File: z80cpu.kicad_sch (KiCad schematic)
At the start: 11 parts

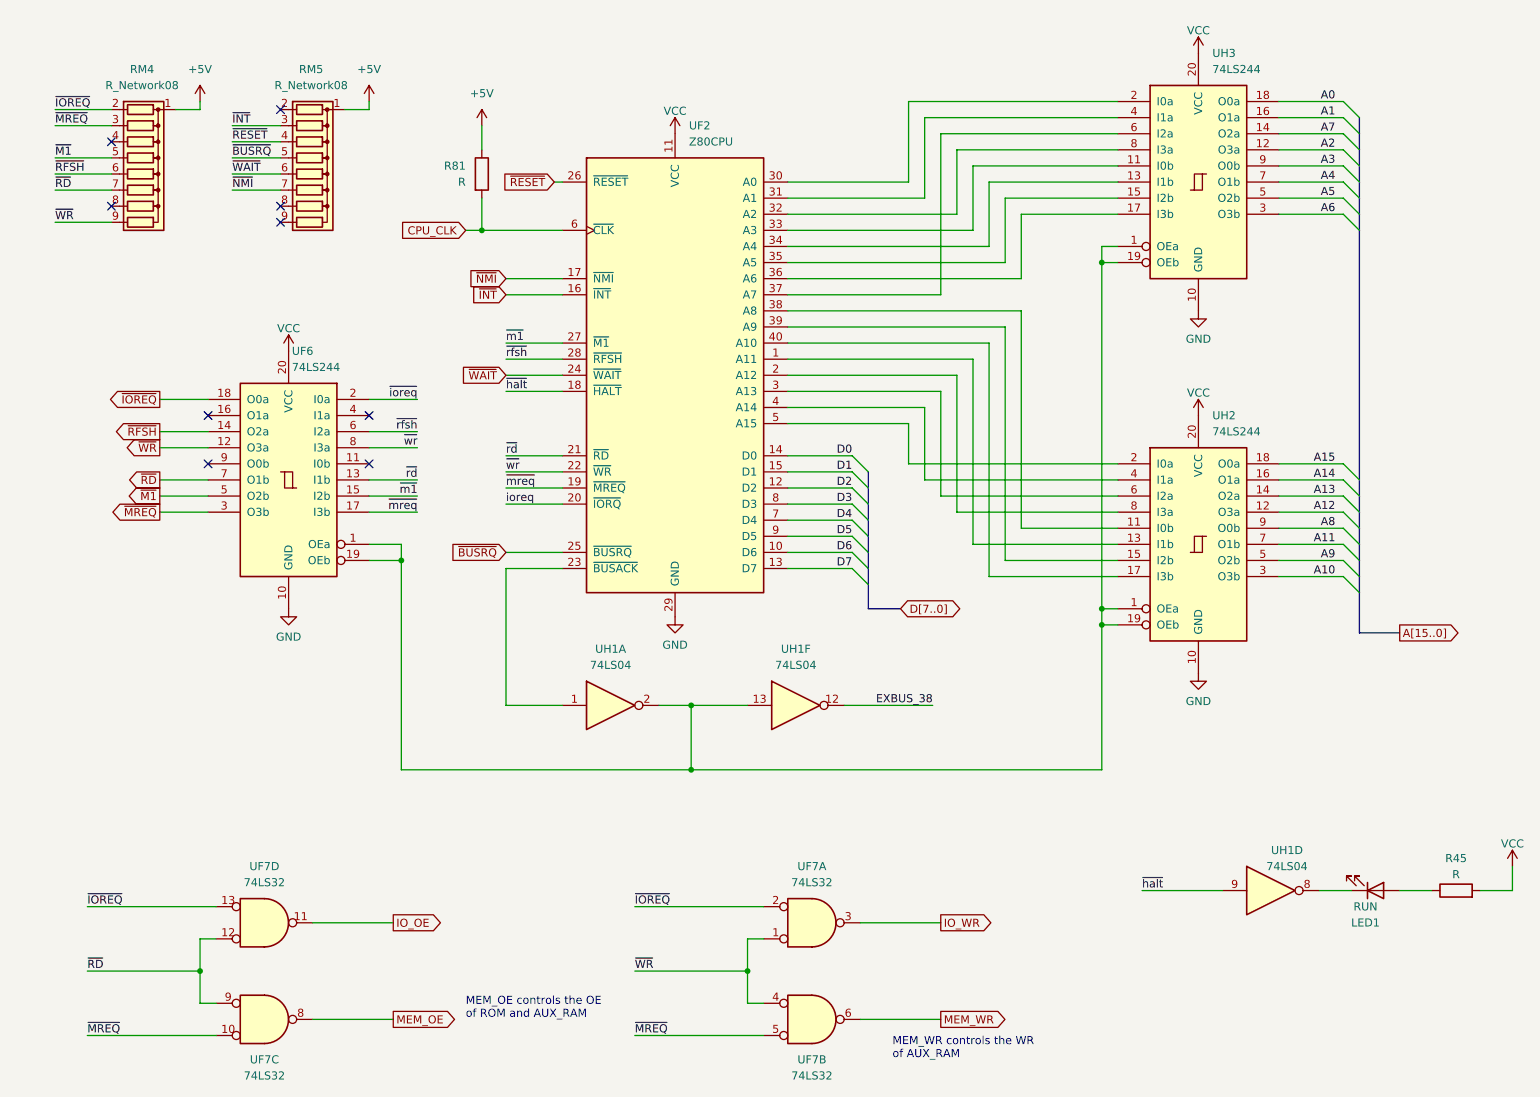
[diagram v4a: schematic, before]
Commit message: VCC -> +5V
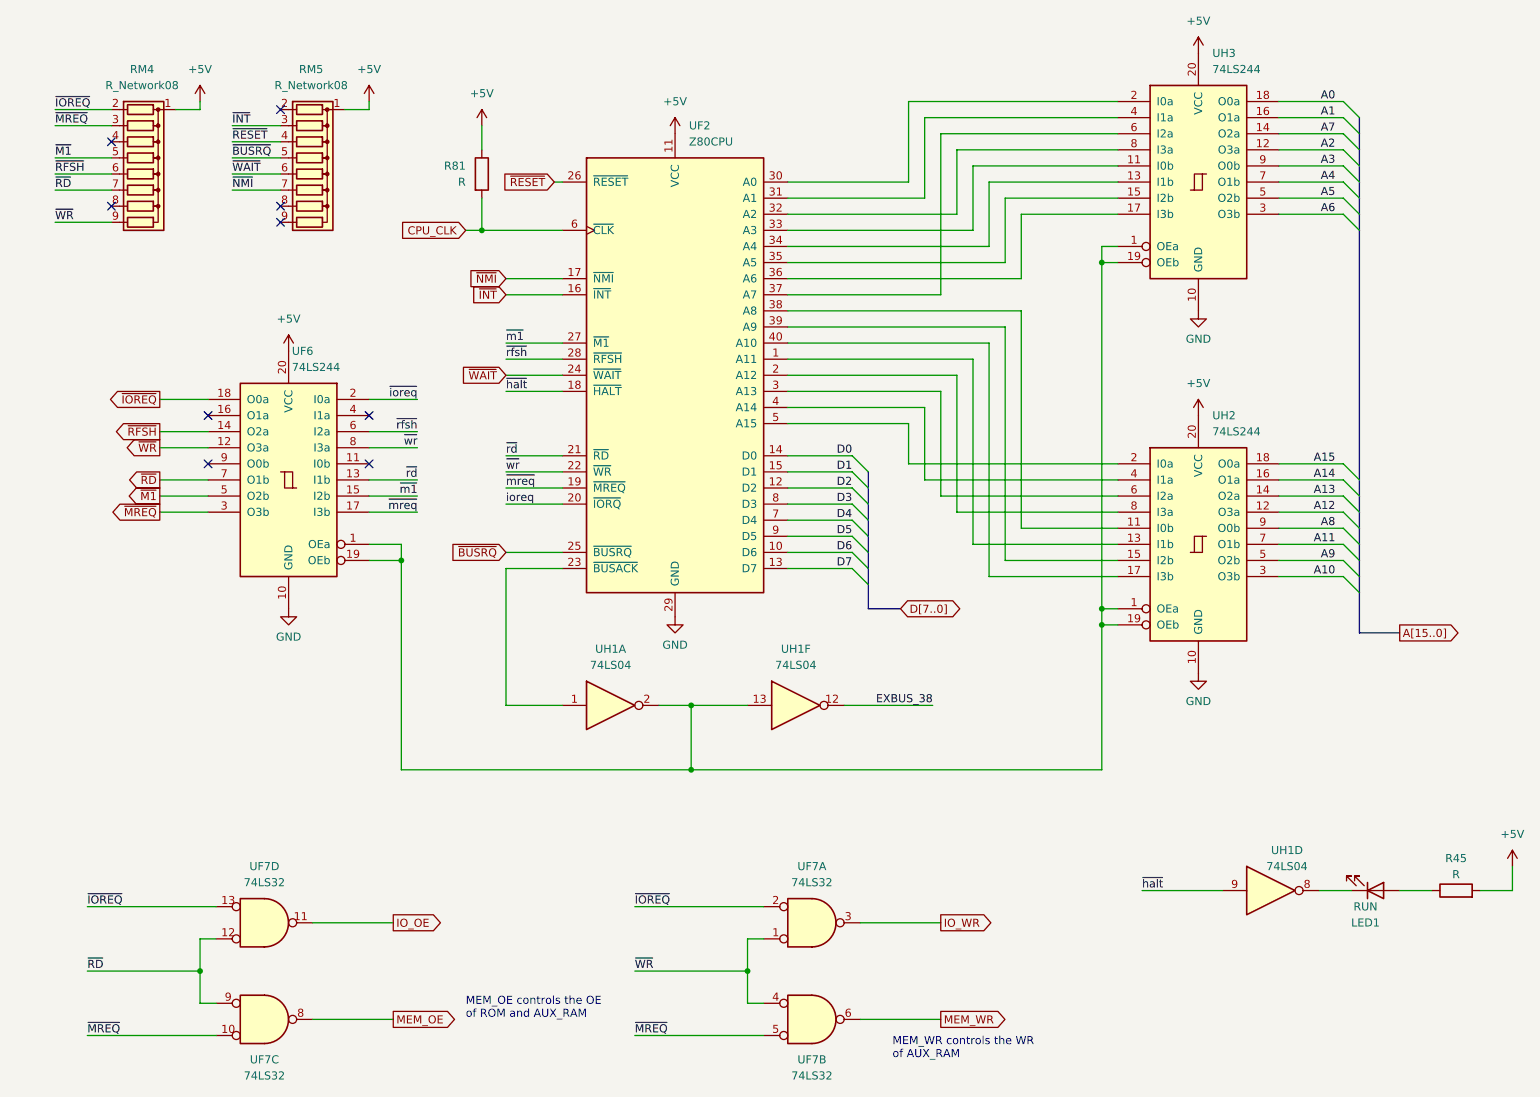
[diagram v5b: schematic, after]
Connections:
- net VCC is gone; now on net +5V: R45.2, UF2.11 (VCC), UF6.20 (VCC), UH2.20 (VCC), UH3.20 (VCC)
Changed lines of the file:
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@@
     )
   )
-  (symbol (lib_id "power:VCC") (at 54.61 68.58 0) (unit 1)
-    (in_bom yes) (on_board yes) (dnp no) (fields_autoplaced)
-    (property "Reference" "#PWR0167" (at 54.61 72.39 0)
-      (effects (font (size 1.27 1.27)) hide)
-    )
-    (property "Value" "VCC" (at 54.61 65.0042 0)
+  (symbol (lib_id "power:+5V") (at 54.61 68.58 0) (unit 1)
+    (in_bom yes) (on_board yes) (dnp no) (fields_autoplaced)
+    (property "Reference" "#PWR?" (at 54.61 72.39 0)
+      (effects (font (size 1.27 1.27)) hide)
+    )
+    (property "Value" "+5V" (at 54.61 63.5 0)
       (effects (font (size 1.27 1.27)))
     )
@@
       (project "ceda"
         (path "/12a6dbe3-008d-4c5b-88f6-9f1c816060be/1847fdc4-53d8-4940-8c5f-7a326599bae2"
-          (reference "#PWR0167") (unit 1)
+          (reference "#PWR?") (unit 1)
         )
       )
@@
     )
   )
-  (symbol (lib_id "power:VCC") (at 115.57 34.29 0) (unit 1)
-    (in_bom yes) (on_board yes) (dnp no) (fields_autoplaced)
-    (property "Reference" "#PWR0163" (at 115.57 38.1 0)
-      (effects (font (size 1.27 1.27)) hide)
-    )
-    (property "Value" "VCC" (at 115.57 30.7142 0)
+  (symbol (lib_id "power:+5V") (at 115.57 34.29 0) (unit 1)
+    (in_bom yes) (on_board yes) (dnp no) (fields_autoplaced)
+    (property "Reference" "#PWR?" (at 115.57 38.1 0)
+      (effects (font (size 1.27 1.27)) hide)
+    )
+    (property "Value" "+5V" (at 115.57 29.21 0)
       (effects (font (size 1.27 1.27)))
     )
@@
       (project "ceda"
         (path "/12a6dbe3-008d-4c5b-88f6-9f1c816060be/1847fdc4-53d8-4940-8c5f-7a326599bae2"
-          (reference "#PWR0163") (unit 1)
+          (reference "#PWR?") (unit 1)
         )
       )
@@
     )
   )
-  (symbol (lib_id "power:VCC") (at 198.12 78.74 0) (unit 1)
-    (in_bom yes) (on_board yes) (dnp no) (fields_autoplaced)
-    (property "Reference" "#PWR0162" (at 198.12 82.55 0)
-      (effects (font (size 1.27 1.27)) hide)
-    )
-    (property "Value" "VCC" (at 198.12 75.1642 0)
+  (symbol (lib_id "power:+5V") (at 198.12 78.74 0) (unit 1)
+    (in_bom yes) (on_board yes) (dnp no) (fields_autoplaced)
+    (property "Reference" "#PWR?" (at 198.12 82.55 0)
+      (effects (font (size 1.27 1.27)) hide)
+    )
+    (property "Value" "+5V" (at 198.12 73.66 0)
       (effects (font (size 1.27 1.27)))
     )
@@
       (project "ceda"
         (path "/12a6dbe3-008d-4c5b-88f6-9f1c816060be/1847fdc4-53d8-4940-8c5f-7a326599bae2"
-          (reference "#PWR0162") (unit 1)
-        )
-      )
-    )
-  )
-  (symbol (lib_id "power:VCC") (at 247.65 149.86 0) (unit 1)
-    (in_bom yes) (on_board yes) (dnp no) (fields_autoplaced)
-    (property "Reference" "#PWR04" (at 247.65 153.67 0)
-      (effects (font (size 1.27 1.27)) hide)
-    )
-    (property "Value" "VCC" (at 247.65 146.2842 0)
+          (reference "#PWR?") (unit 1)
+        )
+      )
+    )
+  )
+  (symbol (lib_id "power:+5V") (at 247.65 149.86 0) (unit 1)
+    (in_bom yes) (on_board yes) (dnp no) (fields_autoplaced)
+    (property "Reference" "#PWR?" (at 247.65 153.67 0)
+      (effects (font (size 1.27 1.27)) hide)
+    )
+    (property "Value" "+5V" (at 247.65 144.78 0)
       (effects (font (size 1.27 1.27)))
     )
@@
       (project "ceda"
         (path "/12a6dbe3-008d-4c5b-88f6-9f1c816060be/1847fdc4-53d8-4940-8c5f-7a326599bae2"
-          (reference "#PWR04") (unit 1)
+          (reference "#PWR?") (unit 1)
         )
       )
@@
     )
   )
-  (symbol (lib_id "power:VCC") (at 198.12 21.59 0) (unit 1)
-    (in_bom yes) (on_board yes) (dnp no) (fields_autoplaced)
-    (property "Reference" "#PWR0165" (at 198.12 25.4 0)
-      (effects (font (size 1.27 1.27)) hide)
-    )
-    (property "Value" "VCC" (at 198.12 18.0142 0)
+  (symbol (lib_id "power:+5V") (at 198.12 21.59 0) (unit 1)
+    (in_bom yes) (on_board yes) (dnp no) (fields_autoplaced)
+    (property "Reference" "#PWR?" (at 198.12 25.4 0)
+      (effects (font (size 1.27 1.27)) hide)
+    )
+    (property "Value" "+5V" (at 198.12 16.51 0)
       (effects (font (size 1.27 1.27)))
     )
@@
       (project "ceda"
         (path "/12a6dbe3-008d-4c5b-88f6-9f1c816060be/1847fdc4-53d8-4940-8c5f-7a326599bae2"
-          (reference "#PWR0165") (unit 1)
-        )
-      )
+          (reference "#PWR?") (unit 1)
+        )
+      )
